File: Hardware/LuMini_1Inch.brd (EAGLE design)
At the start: 28.7 x 28.7 mm, 35 parts, among them J1 DOUBLE_LED_PAD, J2 DOUBLE_LED_PAD, J3 DOUBLE_LED_PAD, J4 DOUBLE_LED_PAD

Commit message: Cleaning repo, changing name, pre review
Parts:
- removed J3: DOUBLE_LED_PAD, Andy:DOUBLELEDPAD
- removed U$3: (no value), buzzard_labels (25):5V6
- removed U$6: (no value), buzzard_labels (25):G4
- added C1: 4.7uF, SparkFun-Capacitors:0603
- added H2, H3: STANDOFF_ELECTRICALSTANDOFF-ELECTRICAL-NOTHERMALS, SparkFun-Hardware:STANDOFF-ELECTRICAL-NOTHERMALS
- U$1: device buzzard_labels (22):CHROMADOT5 -> buzzard_labels (2):LUMINI0
- moved FRAME1 70.3 mm to (-10.2, -6.35)
- moved U$8 2.46 mm to (25.9, 14.3), flipped to the bottom, turned to 288 degrees
- moved U$7 2.35 mm to (25.3, 12.4), flipped to the bottom, turned to 288 degrees
- moved U$4 2.25 mm to (25.0, 18.9), turned to 252 degrees
- moved U$9 2.21 mm to (25.7, 15.5), turned to 270 degrees
- moved U$10 2.19 mm to (25.7, 17.4), turned to 270 degrees
- moved U$5 2.12 mm to (24.5, 20.5), turned to 252 degrees
- moved U$1 0.65 mm to (18.5, 27.2)
- moved J2 0.38 mm to (27.6, 15.3)
- moved J4 0.32 mm to (27.0, 11.3)
- moved J1 0.24 mm to (27.1, 19.1)
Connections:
- net 5V: now also C1.1; no longer D1.VDDPAD, D10.VDDPAD, D11.VDDPAD, D12.VDDPAD, D13.VDDPAD, D14.VDDPAD, D15.VDDPAD, D16.VDDPAD, D17.VDDPAD, D18.VDDPAD, D19.VDDPAD, D2.VDDPAD, D20.VDDPAD, D3.VDDPAD, D4.VDDPAD, D5.VDDPAD, D6.VDDPAD, D7.VDDPAD, D8.VDDPAD, D9.VDDPAD, J3.P$2
- net GND: now also C1.2, H2.P1, H3.P1; no longer D1.GNDPAD, D10.GNDPAD, D11.GNDPAD, D12.GNDPAD, D13.GNDPAD, D14.GNDPAD, D15.GNDPAD, D16.GNDPAD, D17.GNDPAD, D18.GNDPAD, D19.GNDPAD, D2.GNDPAD, D20.GNDPAD, D3.GNDPAD, D4.GNDPAD, D5.GNDPAD, D6.GNDPAD, D7.GNDPAD, D8.GNDPAD, D9.GNDPAD, J3.P$1
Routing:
- net 5V: track 38.0 -> 22.1 mm
- net GND: track 5.96 -> 2.34 mm, vias 3 -> 2
- net N$3: track 4.76 -> 3.52 mm
- net N$41: track 3.16 -> 3.90 mm
- net N$42: track 4.32 -> 3.72 mm
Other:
- outline, holes or cut-outs redrawn
- board text added: "Andy England"
- board text added: "v03"
- board text removed: "v01"

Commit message: adding silk
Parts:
- added LOGO1: SFE_LOGO_NAME.1_INCH, SparkFun-Aesthetics:SFE_LOGO_NAME_.1
- added LOGO2: OSHW-LOGOS, SparkFun-Aesthetics:OSHW-LOGO-S
- added U$11: (no value), buzzard_labels (7):122
- added U$12: (no value), buzzard_labels (7):173
- added U$3: (no value), buzzard_labels (7):20
- added U$6: (no value), buzzard_labels (7):71
- moved U$1 24.9 mm to (12.0, 3.24), turned to 180 degrees
- moved U$2 24.1 mm to (9.91, 4.45), turned to 180 degrees
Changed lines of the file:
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@@
 <setting verticaltext="up"/>
 </settings>
-<grid distance="0.05" unitdist="inch" unit="inch" style="lines" multiple="1" display="yes" altdistance="0.005" altunitdist="inch" altunit="inch"/>
+<grid distance="0.05" unitdist="inch" unit="inch" style="lines" multiple="1" display="yes" altdistance="0.0005" altunitdist="inch" altunit="inch"/>
 <layers>
 <layer number="1" name="Top" color="4" fill="1" visible="yes" active="yes"/>
@@
 <layer number="19" name="Unrouted" color="6" fill="1" visible="yes" active="yes"/>
 <layer number="20" name="Dimension" color="24" fill="1" visible="yes" active="yes"/>
-<layer number="21" name="tPlace" color="7" fill="1" visible="yes" active="yes"/>
+<layer number="21" name="tPlace" color="16" fill="1" visible="yes" active="yes"/>
 <layer number="22" name="bPlace" color="7" fill="1" visible="yes" active="yes"/>
 <layer number="23" name="tOrigins" color="15" fill="1" visible="yes" active="yes"/>
@@
 <element name="J2" library="Andy" package="DOUBLELEDPAD" value="DOUBLE_LED_PAD" x="27.559" y="15.2527" rot="MR270"/>
 <element name="J4" library="Andy" package="DOUBLELEDPAD" value="DOUBLE_LED_PAD" x="26.9875" y="11.2776" rot="MR108"/>
-<element name="U$1" library="buzzard_labels (2)" package="LUMINI0" value="" x="18.4785" y="27.2415" rot="MR0"/>
-<element name="U$2" library="buzzard_labels (22)" package="20_APA102_LED#S6" value="" x="20.574" y="26.035" rot="MR0"/>
+<element name="U$1" library="buzzard_labels (2)" package="LUMINI0" value="" x="12.0015" y="3.2385" rot="MR180"/>
+<element name="U$2" library="buzzard_labels (22)" package="20_APA102_LED#S6" value="" x="9.906" y="4.445" rot="MR180"/>
 <element name="U$4" library="buzzard_labels (25)" package="5V6" value="" x="25.0444" y="18.9103" rot="MR252"/>
 <element name="U$5" library="buzzard_labels (25)" package="G4" value="" x="24.5491" y="20.4978" rot="MR252"/>
@@
 <attribute name="PROD_ID" value="CAP-08280" x="23.368" y="8.255" size="1.778" layer="28" rot="MR130" display="off"/>
 </element>
+<element name="LOGO1" library="SparkFun-Aesthetics" package="SFE_LOGO_NAME_.1" value="SFE_LOGO_NAME.1_INCH" x="15.24" y="26.67" rot="MR0"/>
+<element name="LOGO2" library="SparkFun-Aesthetics" package="OSHW-LOGO-S" value="OSHW-LOGOS" x="3.175" y="15.24" rot="MR270"/>
+<element name="U$3" library="buzzard_labels (7)" package="20" value="" x="25.8064" y="21.2217" rot="MR54"/>
+<element name="U$6" library="buzzard_labels (7)" package="71" value="" x="9.1313" y="25.7302" rot="MR324"/>
+<element name="U$11" library="buzzard_labels (7)" package="122" value="" x="4.5339" y="9.4488" rot="MR234"/>
+<element name="U$12" library="buzzard_labels (7)" package="173" value="" x="21.0185" y="4.5593" rot="MR144"/>
 </elements>
 <signals>

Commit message: Post checklist
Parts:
- removed U$1: (no value), buzzard_labels (2):LUMINI0
- added FD1, FD2, FD3, FD4: FIDUCIALUFIDUCIAL, SparkFun-Aesthetics:FIDUCIAL-MICRO
- added H1, H4: STANDOFF_ELECTRICALSTANDOFF-ELECTRICAL-NOTHERMALS, SparkFun-Hardware:STANDOFF-ELECTRICAL-NOTHERMALS
- added U$13: (no value), SparkFun-Aesthetics:ORDERING_INSTRUCTIONS
- added U$14: (no value), buzzard_labels (8):LUMINI_1#1
- C1: value 4.7uF -> DNP
- moved H2 6.63 mm to (8.26, 21.6)
- moved D12 6.38 mm to (3.12, 17.9)
- moved D20 6.38 mm to (26.1, 17.9)
- moved D3 6.38 mm to (24.4, 28.7)
- moved D6 6.38 mm to (14.6, 33.7)
- moved D9 6.38 mm to (4.85, 28.7)
- moved J1 6.38 mm to (26.4, 25.5)
- moved J4 6.38 mm to (26.4, 17.6)
- moved LOGO1 6.38 mm to (14.6, 33.0)
- moved U$10 6.38 mm to (25.1, 23.7)
- moved U$3 6.38 mm to (25.2, 27.6)
- moved U$4 6.38 mm to (24.4, 25.3)
- moved U$7 6.38 mm to (24.7, 18.7)
- moved U$8 6.38 mm to (25.2, 20.7)
- moved U$9 6.38 mm to (25.1, 21.9)
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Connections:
- net GND: now also H1.P1, H4.P1
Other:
- board size 28.7 x 28.7 mm -> 28.7 x 43.2 mm
- board text added: "Black PCB 2 Oz. Copper"

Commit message: qc checklist changes
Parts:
- D1, D10, D11, D12, D13, D14, D15, D16, D17, D18, D19, D2, D20, D3, D4, D5, D6, D7, D8, D9: value APA1022020 -> APA102-2020
- H1, H2, H3, H4: value STANDOFF_ELECTRICALSTANDOFF-ELECTRICAL-NOTHERMALS -> STANDOFF_ELECTRICAL-NOTHERMALS
- J1, J2, J4: value DOUBLE_LED_PAD -> SOLDER_PAD_2; device Andy:DOUBLELEDPAD -> SparkFun-Connectors:SOLDER_PAD_2
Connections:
- net N$2 renamed CI
- net N$3 renamed DI
- net N$41 renamed CO
- net N$42 renamed DO

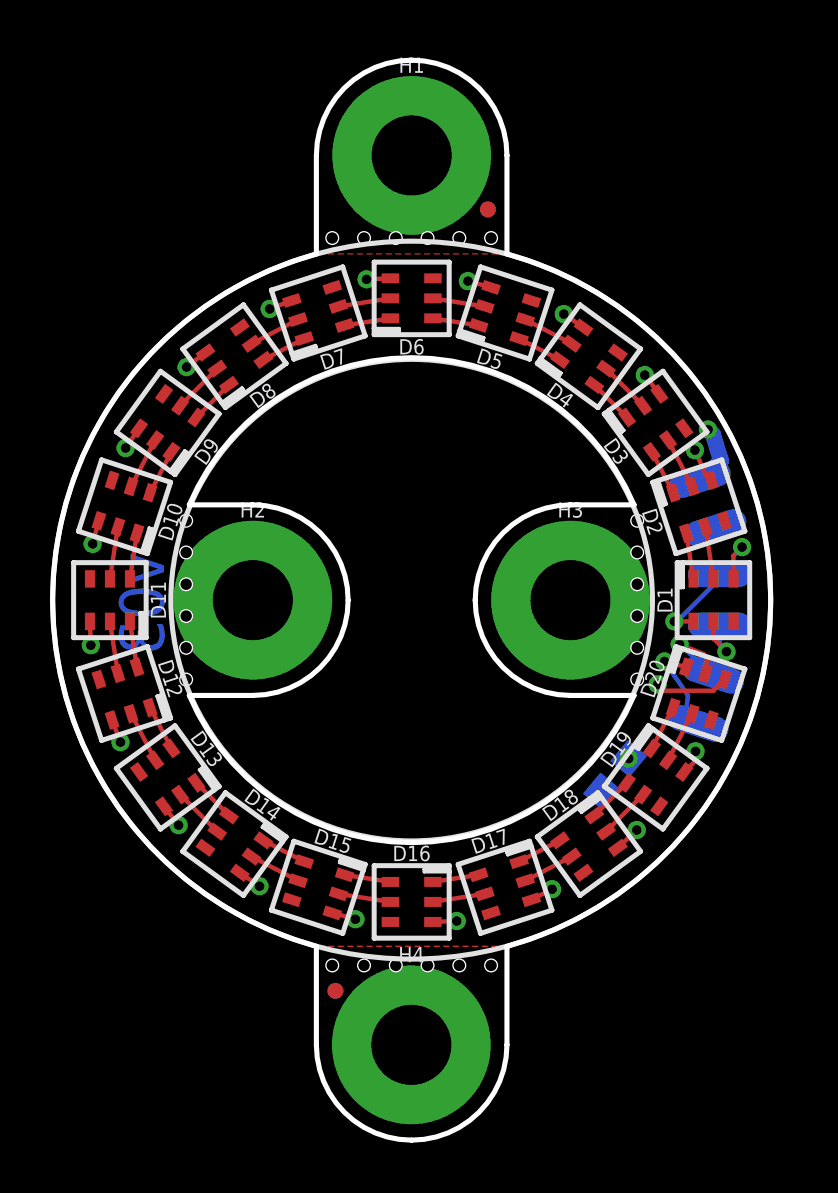
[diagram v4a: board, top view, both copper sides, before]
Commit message: updating to proper footrpint
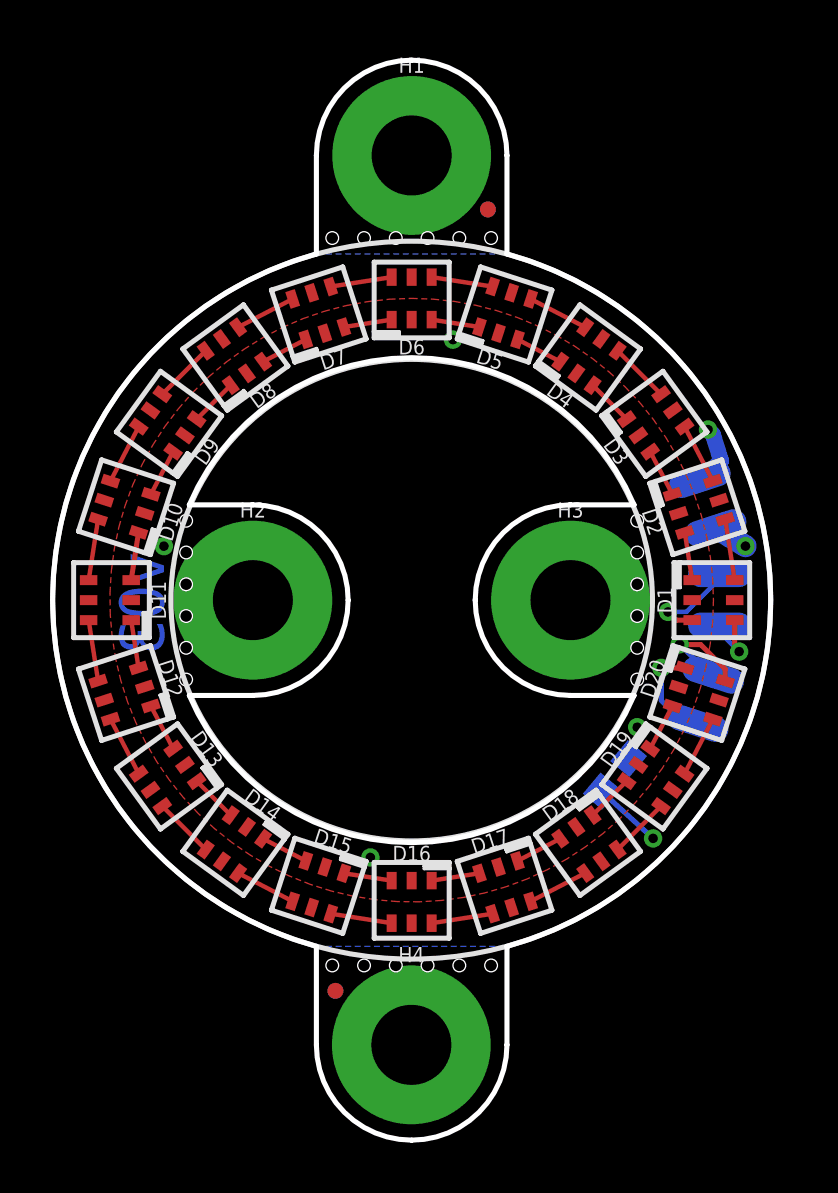
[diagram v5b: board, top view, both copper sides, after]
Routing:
- net 5V: track 22.1 -> 4.21 mm, vias 20 -> 2
- net CO: track 3.67 -> 4.57 mm
- net GND: vias 2 -> 5
- added copper zone on layer 1, net 5V
- added copper zone on layer 16, net GND
- removed copper zone on layer 16, net 5V

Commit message: version number change
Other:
- board text added: "v10"
- board text removed: "v03"
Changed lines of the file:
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@@
 <plain>
 <circle x="14.605" y="21.59" radius="14.351" width="0.2032" layer="21"/>
-<text x="4.699" y="23.495" size="1.778" layer="16" font="vector" ratio="15" rot="SMR270">v03</text>
+<text x="4.699" y="23.495" size="1.778" layer="16" font="vector" ratio="15" rot="SMR270">v10</text>
 <hole x="5.588" y="18.415" drill="0.508"/>
 <wire x1="5.715" y1="17.78" x2="8.255" y2="17.78" width="0.2032" layer="20"/>
